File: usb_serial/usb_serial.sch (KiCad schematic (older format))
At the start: 17 parts, among them P1 USB_OTG, P2 CONN_01X04, P3 CONN_01X04, Q1 S8050, Q2 S8050, U1 CH340G, X1 CRYSTAL_SMD

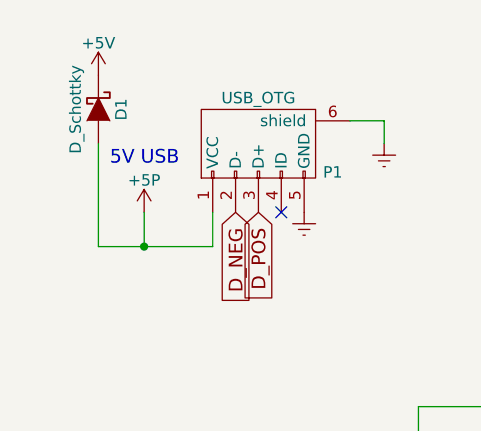
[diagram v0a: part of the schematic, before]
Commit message: Fixes in usb footprints. usb/README.md added.
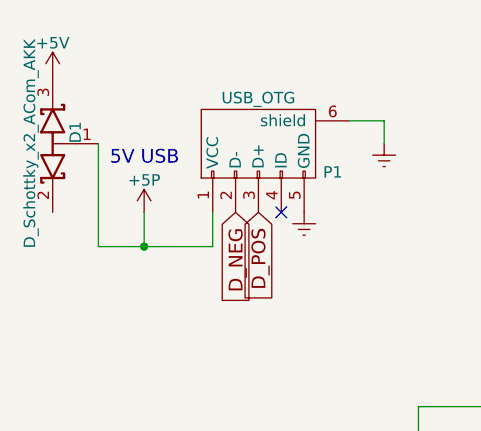
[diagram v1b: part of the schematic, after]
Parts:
- removed D1: D_Schottky, Diodes_SMD:DO-214AB_Handsoldering, symbol D_Schottky
- added D1: D_Schottky_x2_ACom_AKK, TO_SOT_Packages_SMD:SOT-23, symbol D_Schottky_x2_ACom_AKK
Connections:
- net +5P: now also D1.1 (A)
- net +5V: now also D1.3 (K)
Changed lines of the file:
@@
 L +5V #PWR011
 U 1 1 56EEEA7E
-P 2350 1550
-F 0 "#PWR011" H 2350 1400 50  0001 C CNN
-F 1 "+5V" H 2350 1690 50  0000 C CNN
-F 2 "" H 2350 1550 50  0000 C CNN
-F 3 "" H 2350 1550 50  0000 C CNN
-	1    2350 1550
+P 2150 1550
+F 0 "#PWR011" H 2150 1400 50  0001 C CNN
+F 1 "+5V" H 2150 1690 50  0000 C CNN
+F 2 "" H 2150 1550 50  0000 C CNN
+F 3 "" H 2150 1550 50  0000 C CNN
+	1    2150 1550
 	1    0    0    -1
 $EndComp
@@
 	4050 3750 4050 3550
 $Comp
-L D_Schottky D1
-U 1 1 56EEF7A8
-P 2350 1700
-F 0 "D1" H 2350 1800 50  0000 C CNN
-F 1 "D_Schottky" H 2350 1600 50  0000 C CNN
-F 2 "Diodes_SMD:DO-214AB_Handsoldering" H 2350 1700 50  0001 C CNN
-F 3 "" H 2350 1700 50  0000 C CNN
-	1    2350 1700
-	0    1    1    0
+L D_Schottky_x2_ACom_AKK D1
+U 1 1 56EF0076
+P 2150 1850
+F 0 "D1" H 2200 1750 50  0000 C CNN
+F 1 "D_Schottky_x2_ACom_AKK" H 2150 1950 50  0000 C CNN
+F 2 "TO_SOT_Packages_SMD:SOT-23" H 2150 1850 50  0001 C CNN
+F 3 "" H 2150 1850 50  0000 C CNN
+	1    2150 1850
+	0    -1   -1   0
 $EndComp
 $EndSCHEMATC

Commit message: Breakout USB v0 done.
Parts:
- Q1, Q2: footprint TO_SOT_Packages_SMD:SOT-23 -> SOT-23_S8050:SOT-23_S8050
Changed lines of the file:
@@
 F 0 "Q2" H 8350 2975 50  0000 L CNN
 F 1 "S8050" H 8350 2900 50  0000 L CNN
-F 2 "TO_SOT_Packages_SMD:SOT-23" H 8350 2825 50  0000 L CIN
+F 2 "SOT-23_S8050:SOT-23_S8050" H 8350 2825 50  0000 L CIN
 F 3 "" H 8150 2900 50  0000 L CNN
 	1    8150 2900
@@
 F 0 "Q1" H 8350 2225 50  0000 L CNN
 F 1 "S8050" H 8350 2150 50  0000 L CNN
-F 2 "TO_SOT_Packages_SMD:SOT-23" H 8350 2075 50  0000 L CIN
+F 2 "SOT-23_S8050:SOT-23_S8050" H 8350 2075 50  0000 L CIN
 F 3 "" H 8150 2150 50  0000 L CNN
 	1    8150 2150

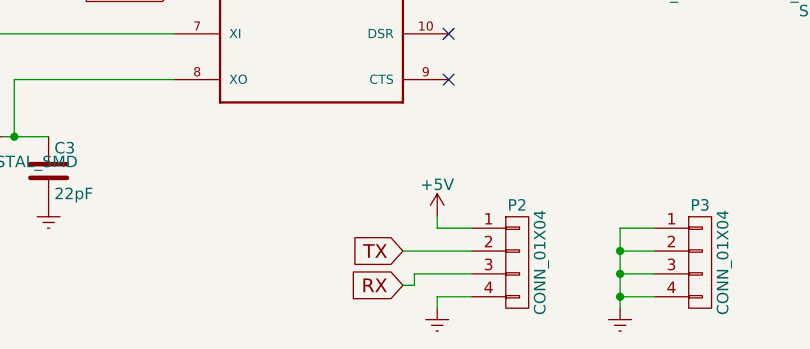
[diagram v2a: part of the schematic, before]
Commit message: Mounting holes & silkscreen with labels
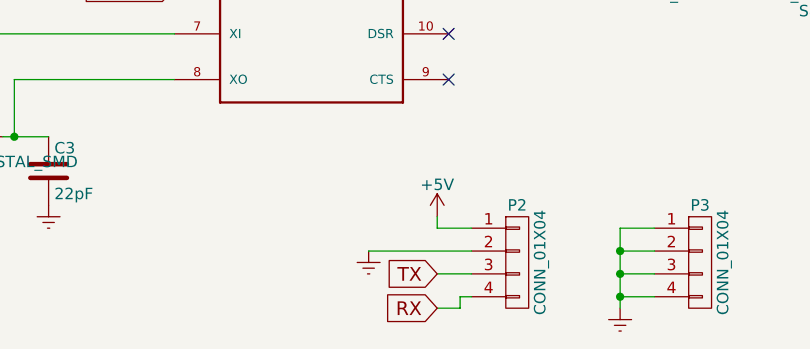
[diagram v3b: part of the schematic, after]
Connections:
- net Earth: now also P2.2 (P2); no longer P2.4 (P4)
- net RX: now also P2.4 (P4); no longer P2.3 (P3)
- net TX: now also P2.3 (P3); no longer P2.2 (P2)
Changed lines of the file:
@@
 L Earth #PWR09
 U 1 1 56EF1D52
-P 6150 4200
-F 0 "#PWR09" H 6150 3950 50  0001 C CNN
-F 1 "Earth" H 6150 4050 50  0001 C CNN
-F 2 "" H 6150 4200 50  0000 C CNN
-F 3 "" H 6150 4200 50  0000 C CNN
-	1    6150 4200
+P 5850 3950
+F 0 "#PWR09" H 5850 3700 50  0001 C CNN
+F 1 "Earth" H 5850 3800 50  0001 C CNN
+F 2 "" H 5850 3950 50  0000 C CNN
+F 3 "" H 5850 3950 50  0000 C CNN
+	1    5850 3950
 	1    0    0    -1
 $EndComp
-Text GLabel 6000 3950 0    60   Input ~ 0
+Text GLabel 6150 4050 0    60   Input ~ 0
 TX
-Text GLabel 6000 4100 0    60   Input ~ 0
+Text GLabel 6150 4200 0    60   Input ~ 0
 RX
 Wire Wire Line
@@
 Wire Wire Line
 	6150 3850 6300 3850
-Wire Wire Line
-	6300 4150 6150 4150
-Wire Wire Line
-	6150 4150 6150 4200
-Wire Wire Line
-	6300 3950 6000 3950
-Wire Wire Line
-	6300 4050 6050 4050
-Wire Wire Line
-	6050 4050 6050 4100
-Wire Wire Line
-	6050 4100 6000 4100
 $Comp
 L Earth #PWR010
@@
 	0    -1   -1   0
 $EndComp
+Wire Wire Line
+	5850 3950 6300 3950
+Wire Wire Line
+	6150 4050 6300 4050
+Wire Wire Line
+	6150 4200 6250 4200
+Wire Wire Line
+	6250 4200 6250 4150
+Wire Wire Line
+	6250 4150 6300 4150
 $EndSCHEMATC

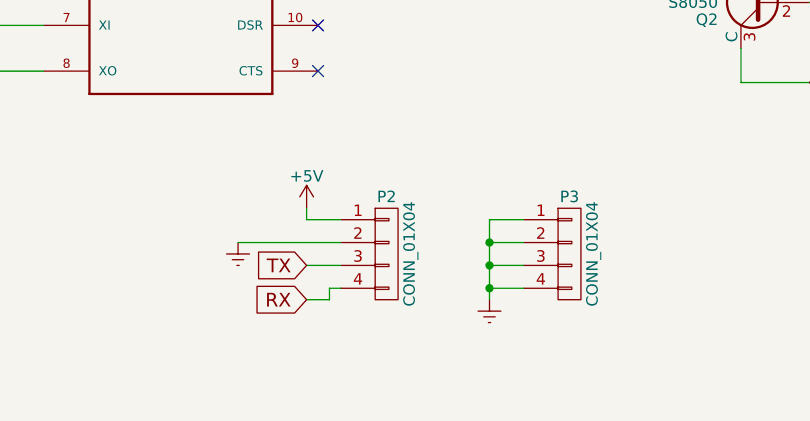
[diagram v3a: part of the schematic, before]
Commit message: Expanded pin headers and minor fixes. Pics updated.
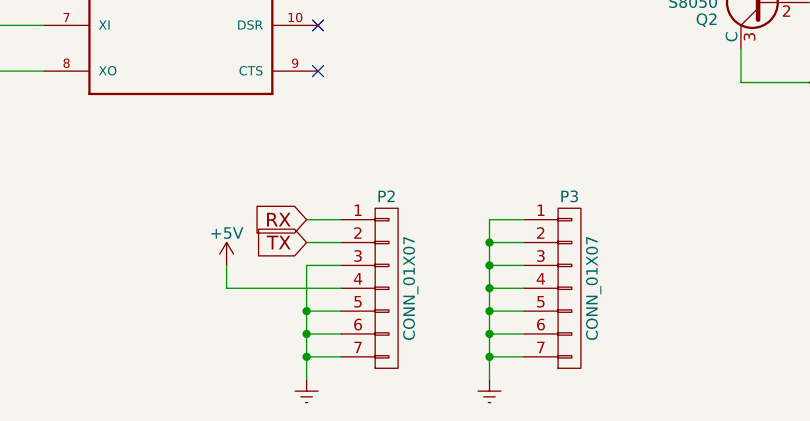
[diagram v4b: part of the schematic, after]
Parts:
- removed P2, P3: CONN_01X04, Pin_Headers:Pin_Header_Straight_1x04, symbol CONN_01X04
- added P2, P3: CONN_01X07, Pin_Headers:Pin_Header_Straight_1x07, symbol CONN_01X07
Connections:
- net +5V: now also P2.4 (P4)
- net Earth: now also P2.3 (P3), P2.5 (P5), P2.6 (P6), P2.7 (P7), P3.1 (P1), P3.2 (P2), P3.3 (P3), P3.4 (P4), P3.5 (P5), P3.6 (P6), P3.7 (P7)
- net RX: now also P2.1 (P1)
- net TX: now also P2.2 (P2)
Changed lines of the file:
@@
 	6300 1550 6300 1800
 Connection ~ 6300 1800
-$Comp
-L CONN_01X04 P2
-U 1 1 56EF185C
-P 6500 4000
-F 0 "P2" H 6500 4250 50  0000 C CNN
-F 1 "CONN_01X04" V 6600 4000 50  0000 C CNN
-F 2 "Pin_Headers:Pin_Header_Straight_1x04" H 6500 4000 50  0001 C CNN
-F 3 "" H 6500 4000 50  0000 C CNN
-	1    6500 4000
-	1    0    0    -1
-$EndComp
-$Comp
-L CONN_01X04 P3
-U 1 1 56EF1951
-P 7300 4000
-F 0 "P3" H 7300 4250 50  0000 C CNN
-F 1 "CONN_01X04" V 7400 4000 50  0000 C CNN
-F 2 "Pin_Headers:Pin_Header_Straight_1x04" H 7300 4000 50  0001 C CNN
-F 3 "" H 7300 4000 50  0000 C CNN
-	1    7300 4000
-	1    0    0    -1
-$EndComp
+Text GLabel 6150 3950 0    60   Input ~ 0
+TX
+Text GLabel 6150 3850 0    60   Input ~ 0
+RX
 $Comp
 L Earth #PWR09
-U 1 1 56EF1D52
-P 5850 3950
-F 0 "#PWR09" H 5850 3700 50  0001 C CNN
-F 1 "Earth" H 5850 3800 50  0001 C CNN
-F 2 "" H 5850 3950 50  0000 C CNN
-F 3 "" H 5850 3950 50  0000 C CNN
-	1    5850 3950
-	1    0    0    -1
-$EndComp
-Text GLabel 6150 4050 0    60   Input ~ 0
-TX
-Text GLabel 6150 4200 0    60   Input ~ 0
-RX
-Wire Wire Line
-	6150 3800 6150 3850
-Wire Wire Line
-	6150 3850 6300 3850
-$Comp
-L Earth #PWR010
 U 1 1 56EF20C2
-P 6950 4200
-F 0 "#PWR010" H 6950 3950 50  0001 C CNN
-F 1 "Earth" H 6950 4050 50  0001 C CNN
-F 2 "" H 6950 4200 50  0000 C CNN
-F 3 "" H 6950 4200 50  0000 C CNN
-	1    6950 4200
+P 6950 4550
+F 0 "#PWR09" H 6950 4300 50  0001 C CNN
+F 1 "Earth" H 6950 4400 50  0001 C CNN
+F 2 "" H 6950 4550 50  0000 C CNN
+F 3 "" H 6950 4550 50  0000 C CNN
+	1    6950 4550
 	1    0    0    -1
 $EndComp
 Wire Wire Line
-	6950 3850 6950 4200
+	6950 3850 6950 4550
 Wire Wire Line
 	6950 3850 7100 3850
@@
 Connection ~ 6950 4150
 $Comp
-L +5V #PWR011
+L +5V #PWR010
 U 1 1 56EEEA7E
 P 2150 1550
-F 0 "#PWR011" H 2150 1400 50  0001 C CNN
+F 0 "#PWR010" H 2150 1400 50  0001 C CNN
 F 1 "+5V" H 2150 1690 50  0000 C CNN
 F 2 "" H 2150 1550 50  0000 C CNN
@@
 	2350 2300 2350 1850
 $Comp
-L +5V #PWR012
+L +5V #PWR011
 U 1 1 56EEEE07
-P 6150 3800
-F 0 "#PWR012" H 6150 3650 50  0001 C CNN
-F 1 "+5V" H 6150 3940 50  0000 C CNN
-F 2 "" H 6150 3800 50  0000 C CNN
-F 3 "" H 6150 3800 50  0000 C CNN
-	1    6150 3800
+P 5800 4050
+F 0 "#PWR011" H 5800 3900 50  0001 C CNN
+F 1 "+5V" H 5800 4190 50  0000 C CNN
+F 2 "" H 5800 4050 50  0000 C CNN
+F 3 "" H 5800 4050 50  0000 C CNN
+	1    5800 4050
 	1    0    0    -1
 $EndComp
 $Comp
-L +5V #PWR013
+L +5V #PWR012
 U 1 1 56EEEF41
 P 6300 1550
-F 0 "#PWR013" H 6300 1400 50  0001 C CNN
+F 0 "#PWR012" H 6300 1400 50  0001 C CNN
 F 1 "+5V" H 6300 1690 50  0000 C CNN
 F 2 "" H 6300 1550 50  0000 C CNN
@@
 $EndComp
 $Comp
-L +5P #PWR014
+L +5P #PWR013
 U 1 1 56EEF025
 P 2550 2150
-F 0 "#PWR014" H 2550 2000 50  0001 C CNN
+F 0 "#PWR013" H 2550 2000 50  0001 C CNN
 F 1 "+5P" H 2550 2290 50  0000 C CNN
 F 2 "" H 2550 2150 50  0000 C CNN
@@
 $EndComp
 $Comp
-L Earth #PWR015
+L Earth #PWR014
 U 1 1 56EEF4D5
 P 4050 3750
-F 0 "#PWR015" H 4050 3500 50  0001 C CNN
+F 0 "#PWR014" H 4050 3500 50  0001 C CNN
 F 1 "Earth" H 4050 3600 50  0001 C CNN
 F 2 "" H 4050 3750 50  0000 C CNN
@@
 	0    -1   -1   0
 $EndComp
+$Comp
+L CONN_01X07 P2
+U 1 1 56F43359
+P 6500 4150
+F 0 "P2" H 6500 4550 50  0000 C CNN
+F 1 "CONN_01X07" V 6600 4150 50  0000 C CNN
+F 2 "Pin_Headers:Pin_Header_Straight_1x07" H 6500 4150 50  0001 C CNN
+F 3 "" H 6500 4150 50  0000 C CNN
+	1    6500 4150
+	1    0    0    -1
+$EndComp
+$Comp
+L CONN_01X07 P3
+U 1 1 56F433C8
+P 7300 4150
+F 0 "P3" H 7300 4550 50  0000 C CNN
+F 1 "CONN_01X07" V 7400 4150 50  0000 C CNN
+F 2 "Pin_Headers:Pin_Header_Straight_1x07" H 7300 4150 50  0001 C CNN
+F 3 "" H 7300 4150 50  0000 C CNN
+	1    7300 4150
+	1    0    0    -1
+$EndComp
 Wire Wire Line
-	5850 3950 6300 3950
+	7100 4250 6950 4250
+Connection ~ 6950 4250
+Wire Wire Line
+	7100 4350 6950 4350
+Connection ~ 6950 4350
+Wire Wire Line
+	7100 4450 6950 4450
+Connection ~ 6950 4450
+$Comp
+L Earth #PWR015
+U 1 1 56F435BB
+P 6150 4550
+F 0 "#PWR015" H 6150 4300 50  0001 C CNN
+F 1 "Earth" H 6150 4400 50  0001 C CNN
+F 2 "" H 6150 4550 50  0000 C CNN
+F 3 "" H 6150 4550 50  0000 C CNN
+	1    6150 4550
+	1    0    0    -1
+$EndComp
+Wire Wire Line
+	6150 4050 6150 4550
+Wire Wire Line
+	6150 4450 6300 4450
+Wire Wire Line
+	6150 4250 6300 4250
+Connection ~ 6150 4450
+Wire Wire Line
+	6300 4350 6150 4350
+Connection ~ 6150 4350
+Wire Wire Line
+	6150 3850 6300 3850
+Wire Wire Line
+	6150 3950 6300 3950
+Connection ~ 6150 4250
 Wire Wire Line
 	6150 4050 6300 4050
 Wire Wire Line
-	6150 4200 6250 4200
+	5800 4050 5800 4150
 Wire Wire Line
-	6250 4200 6250 4150
-Wire Wire Line
-	6250 4150 6300 4150
+	5800 4150 6300 4150
 $EndSCHEMATC
